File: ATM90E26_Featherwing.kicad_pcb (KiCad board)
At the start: 2 copper layers, 49.9 x 39.4 mm, 59 parts, among them J1 ST-PJ-312, J2 4P-SMD-2.0-90D, J3 4P-SMD-2.0-90D, J4 12V AC, Q1 8.192MHz, U1 ATM90E26, U2 CJT1117-5.0-SOT223

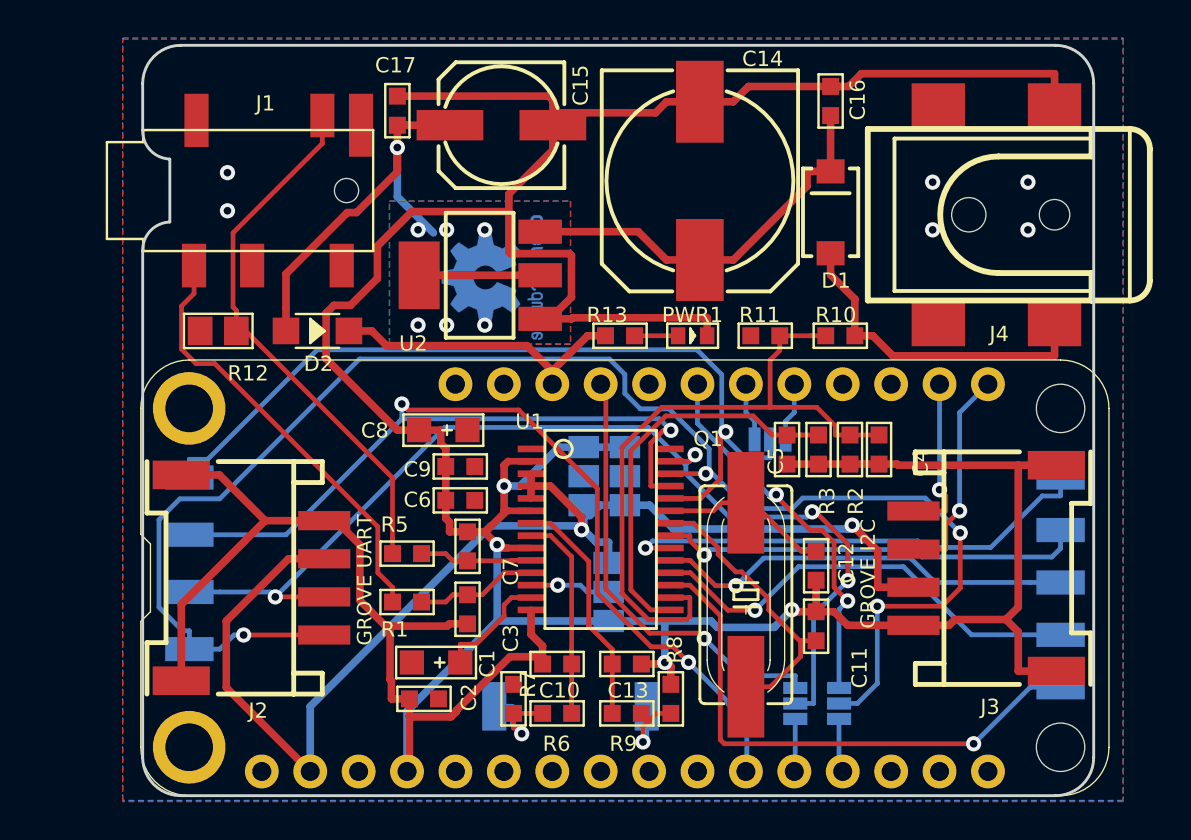
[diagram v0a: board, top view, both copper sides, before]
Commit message: Fixed dangling/disconnected nodes
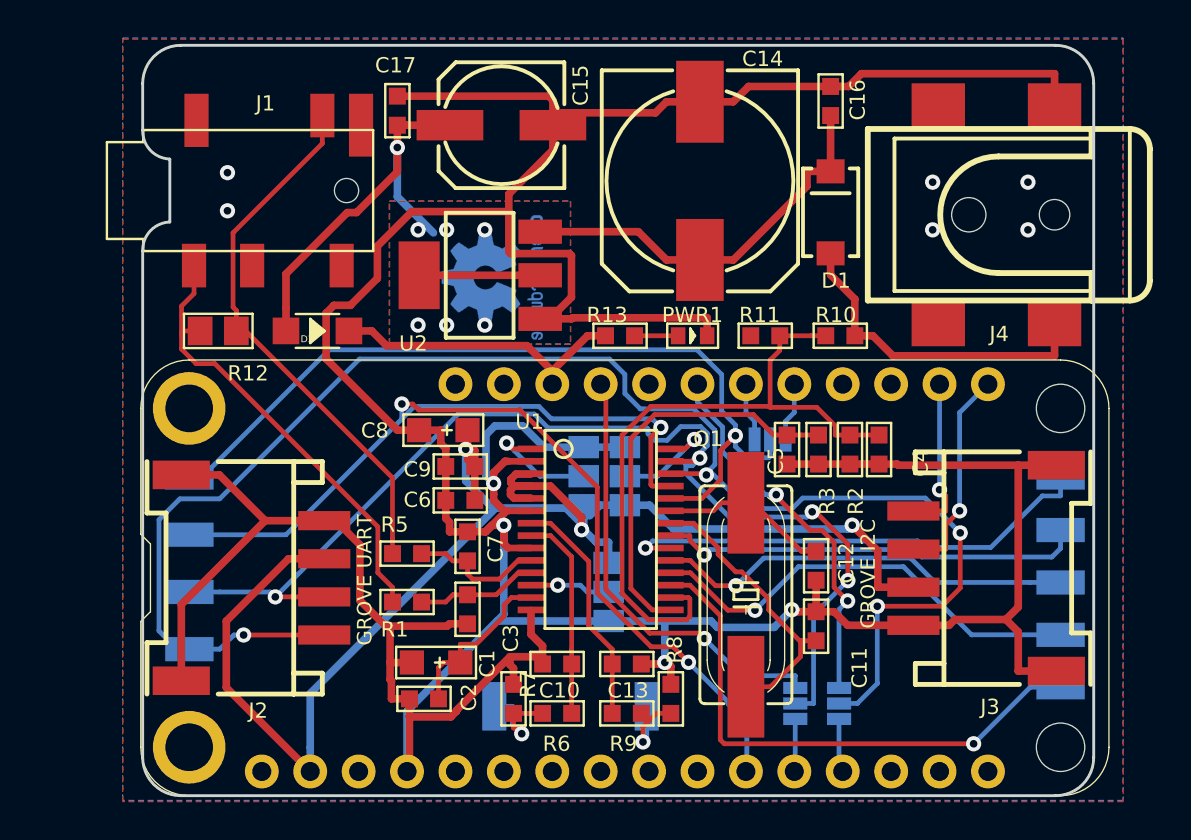
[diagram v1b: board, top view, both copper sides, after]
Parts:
- C7: footprint C0603 -> ATM90E26_Featherwing:C0603
- D2: footprint SOD-123 -> ATM90E26_Featherwing:SOD-123
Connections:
- C1 pad -: Net-(C1-Pad-) -> GND
- C2 pad 2: Net-(C2-Pad2) -> Net-(C1-Pad+)
- C6 pad 2: Net-(C6-Pad2) -> +3V3
- C8 pad +: Net-(C8-Pad+) -> +3V3
- C9 pad 1: Net-(C9-Pad1) -> +3V3
- R12 pad 1: Net-(R12-Pad1) -> /I1P_IN
- R7 pad 1: Net-(R7-Pad1) -> GND
- U1 pad 1: Net-(U1-Pad1) -> Net-(MMD1-Pad2)
- U1 pad 28: Net-(U1-Pad28) -> Net-(MMD0-Pad2)
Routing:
- net +3V3: track 67.8 -> 81.8 mm, vias 2 -> 3
- net GND: track 236.2 -> 244.9 mm
- net Net-(MMD1-Pad2): track 0.00 -> 6.17 mm, vias 0 -> 1
- net Net-(MMD0-Pad2): track 0.00 -> 5.91 mm, vias 0 -> 1
- net /SI/RX: track 56.2 -> 60.5 mm
- net Net-(C1-Pad+): track 6.03 -> 8.93 mm
- net /SO/TX: track 82.3 -> 83.6 mm
- net /I1N: track 5.91 -> 7.11 mm
- net /I1P_IN: track 23.1 -> 24.2 mm
- net /CS: track 44.6 -> 44.0 mm
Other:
- board text added: "30/04/2018"
- board text added: "v 1.4"
- board text removed: "27/02/2018"
- board text removed: "v 1.3"

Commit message: pcb: connect R11 to ground
Signed-off-by: Eliot Blennerhassett <eliot@blennerhassett.gen.nz>
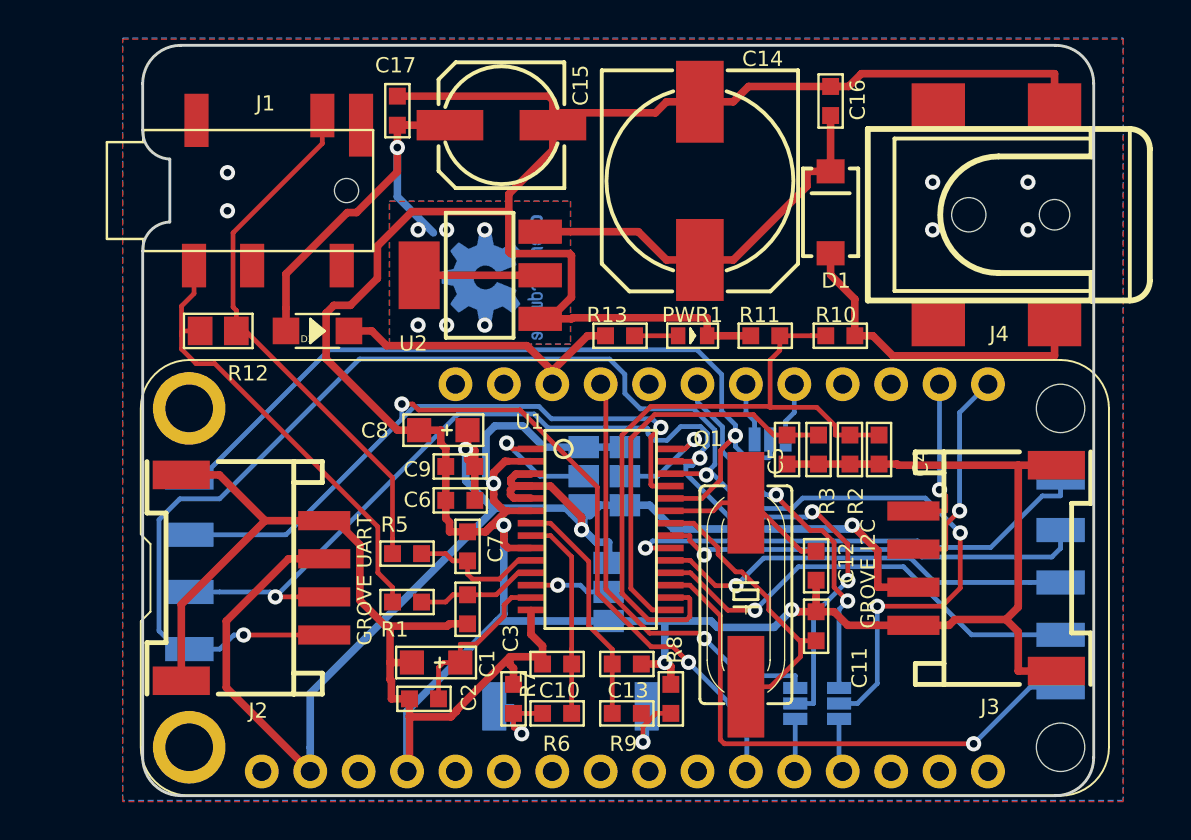
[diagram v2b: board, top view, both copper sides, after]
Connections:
- R11 pad 2: Net-(R11-Pad2) -> GND
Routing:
- net GND: track 244.9 -> 247.1 mm

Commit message: Successfully fabricated and merged with 3-pin stereo (#2)
* Converted to SJ-3525 for current clamp input

* Add stitchig vias

* New gerbers and git ignore of temp files

Signed-off-by: Tisham Dhar <whatnickd@gmail.com>
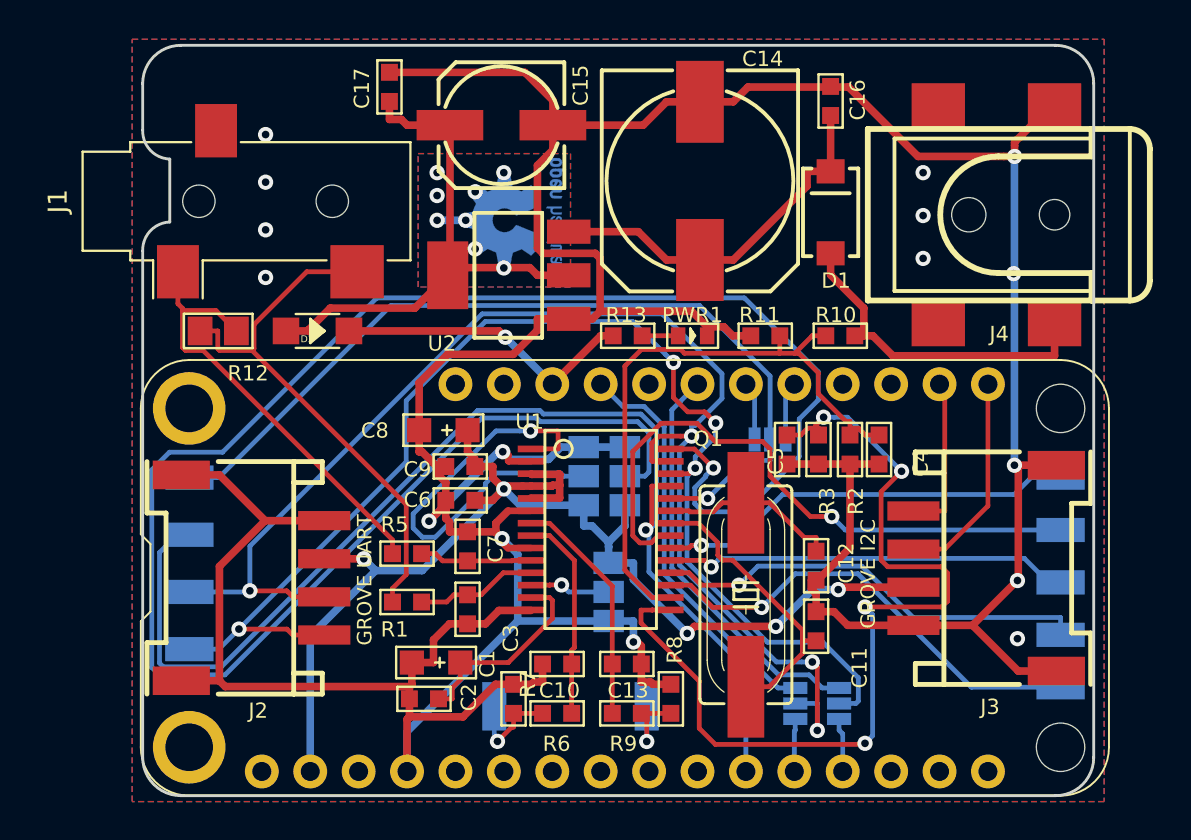
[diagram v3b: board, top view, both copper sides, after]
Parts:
- J1: value ST-PJ-312 -> AudioJack3; footprint ATM90E26_Featherwing:AUDIO6P-SMD-3.5-14.0X6.4X5.0MM -> Connector_Audio:Jack_3.5mm_CUI_SJ-3523-SMT_Horizontal
- moved J1 7.35 mm to (129.0, 93.5), turned to 90 degrees
- moved LOGO1 3.16 mm to (143.0, 94.5)
- moved U2 1.50 mm to (142.7, 97.4)
- moved C17 1.31 mm to (136.5, 87.5)
- moved R13 0.40 mm to (149.0, 100.6)
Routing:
- net Net-(MMD0-Pad2): track 5.91 -> 102.9 mm
- net /VN: track 21.2 -> 48.6 mm, vias 0 -> 4
- net Net-(MMD1-Pad2): track 6.17 -> 23.3 mm
- net /SO/TX: track 83.6 -> 67.6 mm
- net +3V3: track 81.8 -> 66.7 mm, vias 3 -> 5
- net /SI/RX: track 60.5 -> 71.3 mm
- net Net-(U1-Pad21): track 22.5 -> 32.9 mm
- net GND: track 247.1 -> 239.8 mm, vias 10 -> 16
- net /I1N_IN: track 28.7 -> 23.3 mm
- net Net-(U1-Pad17): track 29.0 -> 24.2 mm
- net /5V_REG: track 27.9 -> 32.6 mm, vias 7 -> 8
- net /I1P_IN: track 24.2 -> 28.5 mm
- net Net-(INT1-Pad1): track 25.5 -> 22.0 mm
- net /VP: track 35.9 -> 33.4 mm
- net /CS: track 44.0 -> 46.2 mm
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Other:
- board text added: "16/06/2019"
- board text added: "v 1.5"
- board text removed: "30/04/2018"
- board text removed: "v 1.4"
